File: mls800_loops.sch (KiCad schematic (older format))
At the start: 52 parts, among them J10 JACK_2P_STACK, J11 JACK_2P_SW, J2 JACK_2P_SW, J3 JACK_2P_STACK, J4 JACK_2P_STACK, J5 JACK_2P_STACK, J6 JACK_2P_STACK, J7 JACK_2P_STACK, J8 JACK_2P_STACK, J9 JACK_2P_STACK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

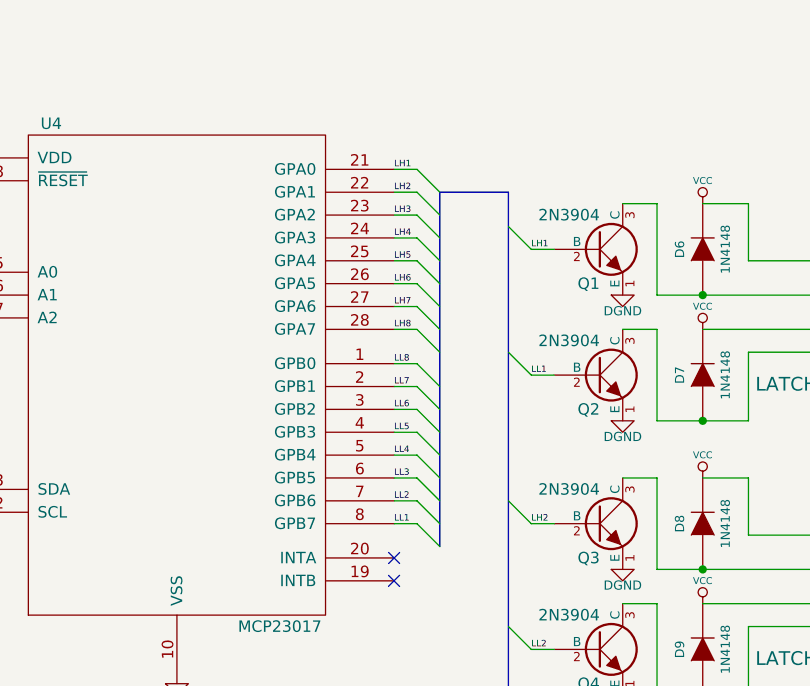
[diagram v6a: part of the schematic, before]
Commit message: MLS800
* routing : core pcb & components
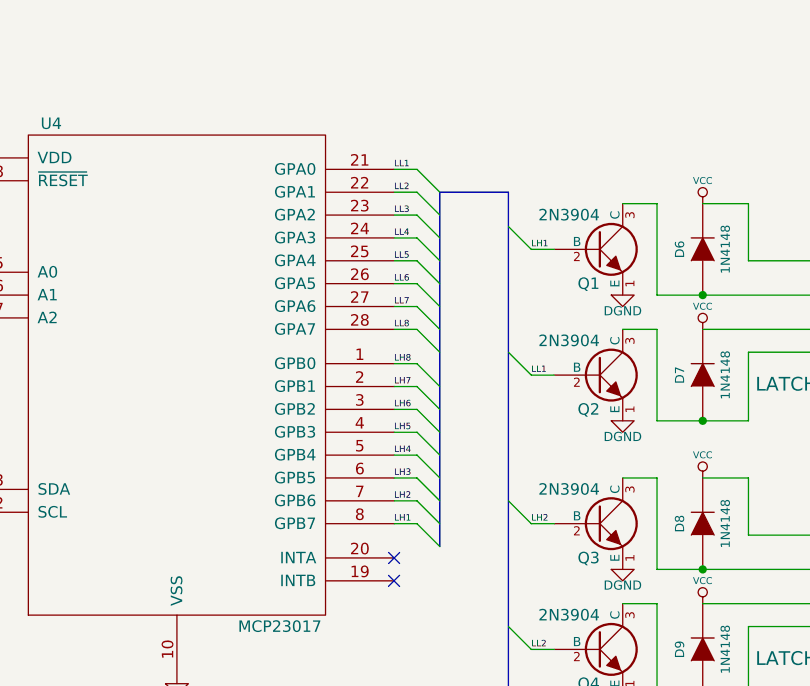
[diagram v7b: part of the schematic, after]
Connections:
- net LH1: now also U4.8 (GPB7); no longer U4.21 (GPA0)
- net LH2: now also U4.7 (GPB6); no longer U4.22 (GPA1)
- net LH3: now also U4.6 (GPB5); no longer U4.23 (GPA2)
- net LH4: now also U4.5 (GPB4); no longer U4.24 (GPA3)
- net LH5: now also U4.4 (GPB3); no longer U4.25 (GPA4)
- net LH6: now also U4.3 (GPB2); no longer U4.26 (GPA5)
- net LH7: now also U4.2 (GPB1); no longer U4.27 (GPA6)
- net LH8: now also U4.1 (GPB0); no longer U4.28 (GPA7)
- net LL1: now also U4.21 (GPA0); no longer U4.8 (GPB7)
- net LL2: now also U4.22 (GPA1); no longer U4.7 (GPB6)
- net LL3: now also U4.23 (GPA2); no longer U4.6 (GPB5)
- net LL4: now also U4.24 (GPA3); no longer U4.5 (GPB4)
- net LL5: now also U4.25 (GPA4); no longer U4.4 (GPB3)
- net LL6: now also U4.26 (GPA5); no longer U4.3 (GPB2)
- net LL7: now also U4.27 (GPA6); no longer U4.2 (GPB1)
- net LL8: now also U4.28 (GPA7); no longer U4.1 (GPB0)
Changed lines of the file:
@@
 	3100 1100 3200 1200
 Text Label 3000 1100 0    28   ~ 0
+LL1
+Text Label 3000 1200 0    28   ~ 0
+LL2
+Text Label 3000 1300 0    28   ~ 0
+LL3
+Text Label 3000 1400 0    28   ~ 0
+LL4
+Text Label 3000 1500 0    28   ~ 0
+LL5
+Text Label 3000 1600 0    28   ~ 0
+LL6
+Text Label 3000 1700 0    28   ~ 0
+LL7
+Text Label 3000 1800 0    28   ~ 0
+LL8
+Text Label 3000 1950 0    28   ~ 0
+LH8
+Text Label 3000 2050 0    28   ~ 0
+LH7
+Text Label 3000 2150 0    28   ~ 0
+LH6
+Text Label 3000 2250 0    28   ~ 0
+LH5
+Text Label 3000 2350 0    28   ~ 0
+LH4
+Text Label 3000 2450 0    28   ~ 0
+LH3
+Text Label 3000 2550 0    28   ~ 0
+LH2
+Text Label 3000 2650 0    28   ~ 0
 LH1
-Text Label 3000 1200 0    28   ~ 0
-LH2
-Text Label 3000 1300 0    28   ~ 0
-LH3
-Text Label 3000 1400 0    28   ~ 0
-LH4
-Text Label 3000 1500 0    28   ~ 0
-LH5
-Text Label 3000 1600 0    28   ~ 0
-LH6
-Text Label 3000 1700 0    28   ~ 0
-LH7
-Text Label 3000 1800 0    28   ~ 0
-LH8
-Text Label 3000 1950 0    28   ~ 0
-LL8
-Text Label 3000 2050 0    28   ~ 0
-LL7
-Text Label 3000 2150 0    28   ~ 0
-LL6
-Text Label 3000 2250 0    28   ~ 0
-LL5
-Text Label 3000 2350 0    28   ~ 0
-LL4
-Text Label 3000 2450 0    28   ~ 0
-LL3
-Text Label 3000 2550 0    28   ~ 0
-LL2
-Text Label 3000 2650 0    28   ~ 0
-LL1
 Text Notes 850  5850 0    197  ~ 39
 LOOPS

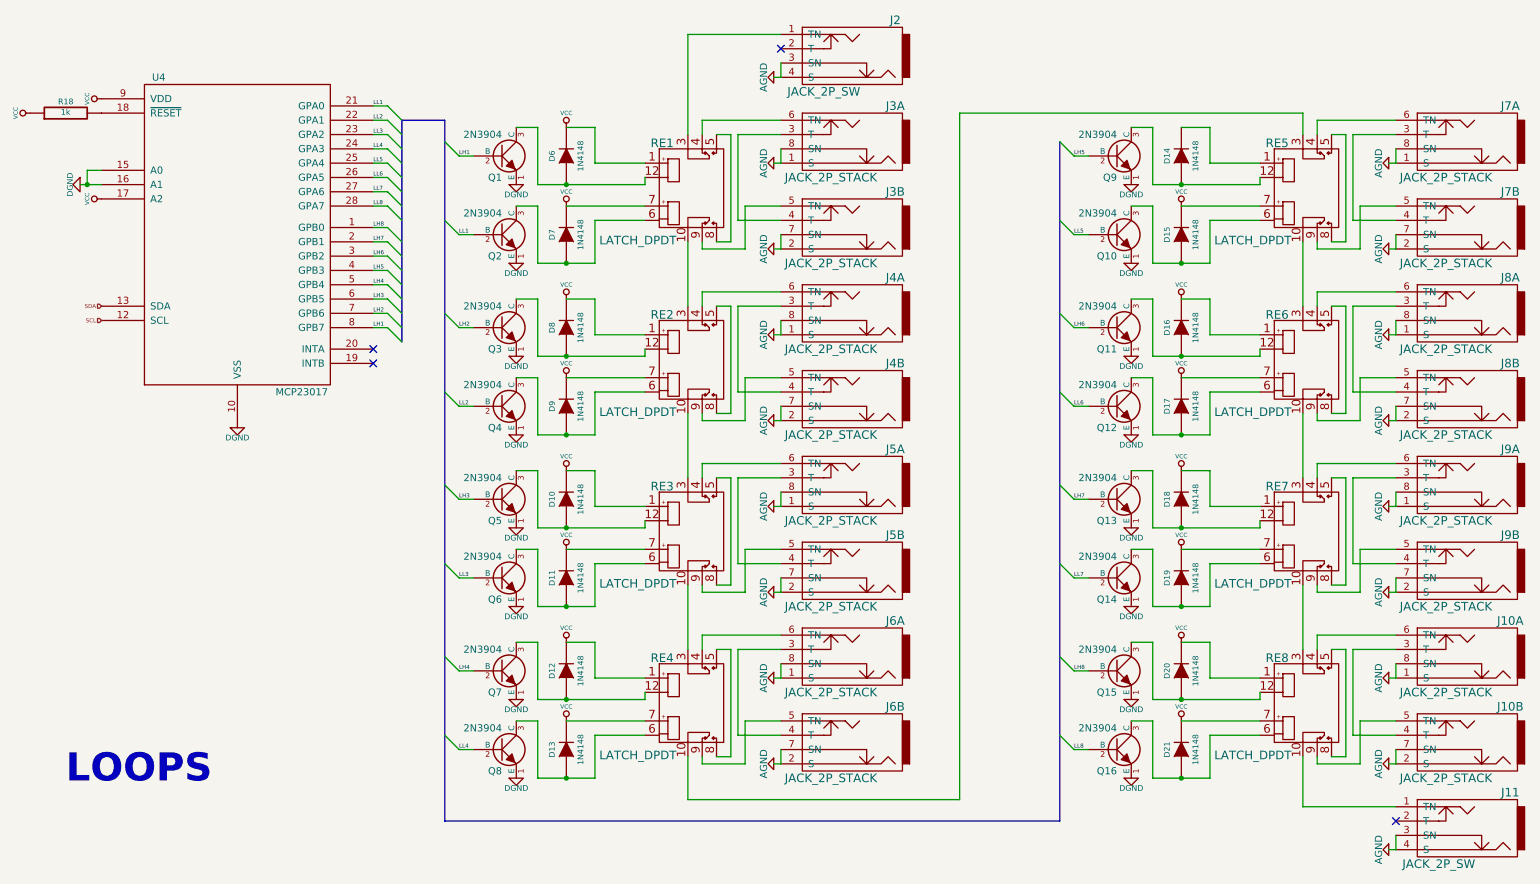
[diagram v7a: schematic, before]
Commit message: MLS800
* schematic : changed all 1n4148 to bournes references
 * changed footprints to match bournes ones
 * re routed all the loops part of the pcb
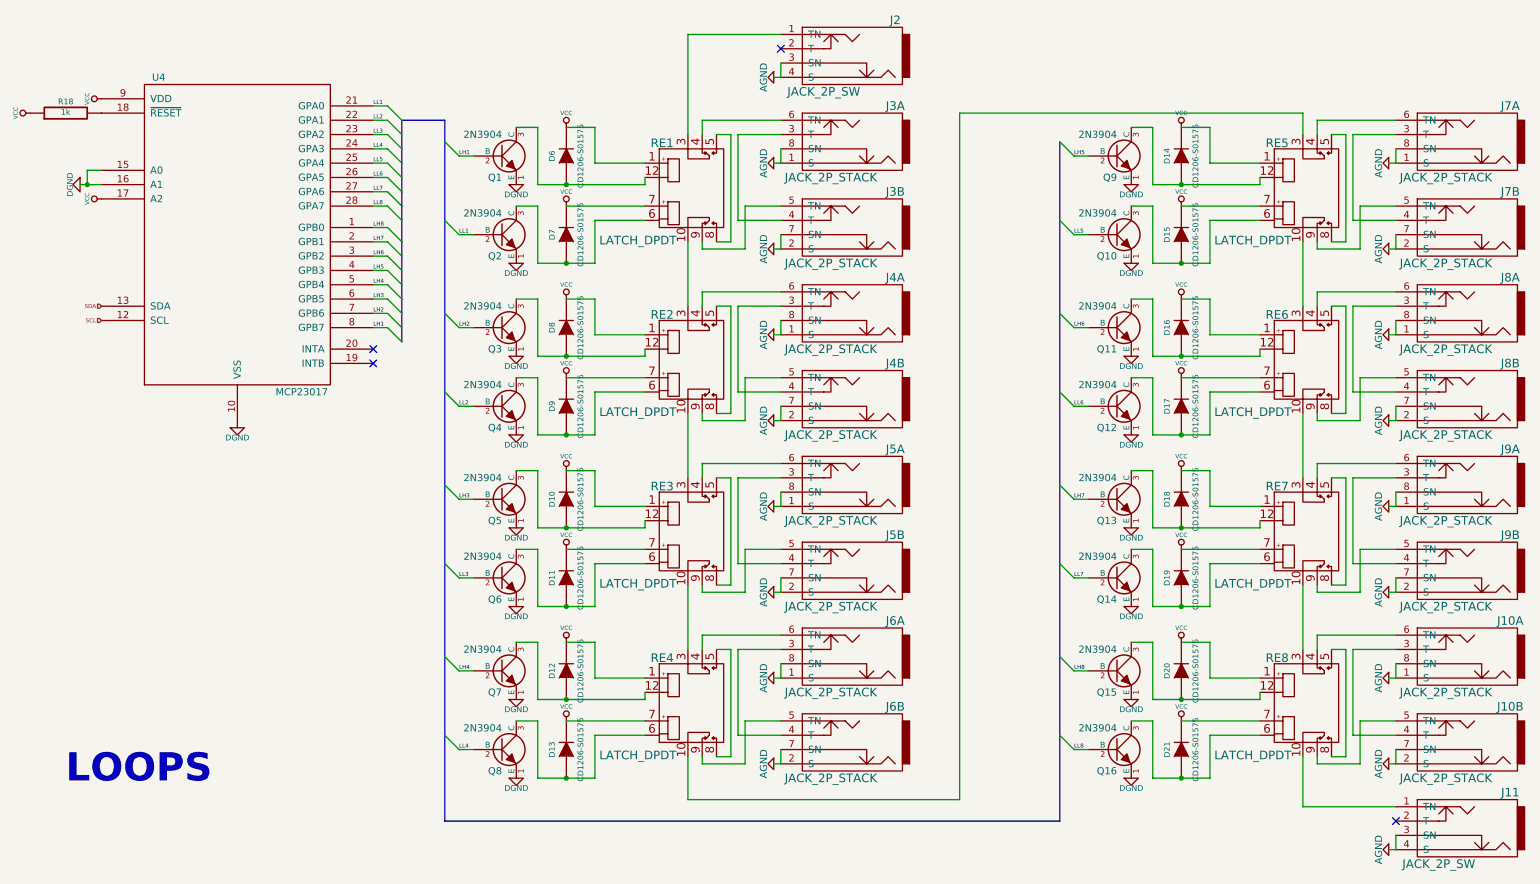
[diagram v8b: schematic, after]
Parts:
- D10, D11, D12, D13, D14, D15, D16, D17, D18, D19, D20, D21, D6, D7, D8, D9: value 1N4148 -> CD1206-S01575; footprint Imported:SOD-123 -> SMD_Packages:SMD-1206_Pol
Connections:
- net VCC: now also D14.2 (K), RE5.1
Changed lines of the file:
@@
 P 4350 1450
 F 0 "D6" H 4350 1550 40  0000 C CNN
-F 1 "1N4148" H 4350 1350 40  0000 C CNN
-F 2 "Imported:SOD-123" H 4350 1450 60  0001 C CNN
+F 1 "CD1206-S01575" H 4350 1350 40  0000 C CNN
+F 2 "SMD_Packages:SMD-1206_Pol" H 4350 1450 60  0001 C CNN
 F 3 "~" H 4350 1450 60  0000 C CNN
 	1    4350 1450
@@
 P 4350 2000
 F 0 "D7" H 4350 2100 40  0000 C CNN
-F 1 "1N4148" H 4350 1900 40  0000 C CNN
-F 2 "Imported:SOD-123" H 4350 2000 60  0001 C CNN
+F 1 "CD1206-S01575" H 4350 1900 40  0000 C CNN
+F 2 "SMD_Packages:SMD-1206_Pol" H 4350 2000 60  0001 C CNN
 F 3 "~" H 4350 2000 60  0000 C CNN
 	1    4350 2000
@@
 P 4350 2650
 F 0 "D8" H 4350 2750 40  0000 C CNN
-F 1 "1N4148" H 4350 2550 40  0000 C CNN
-F 2 "Imported:SOD-123" H 4350 2650 60  0001 C CNN
+F 1 "CD1206-S01575" H 4350 2550 40  0000 C CNN
+F 2 "SMD_Packages:SMD-1206_Pol" H 4350 2650 60  0001 C CNN
 F 3 "~" H 4350 2650 60  0000 C CNN
 	1    4350 2650
@@
 P 4350 3200
 F 0 "D9" H 4350 3300 40  0000 C CNN
-F 1 "1N4148" H 4350 3100 40  0000 C CNN
-F 2 "Imported:SOD-123" H 4350 3200 60  0001 C CNN
+F 1 "CD1206-S01575" H 4350 3100 40  0000 C CNN
+F 2 "SMD_Packages:SMD-1206_Pol" H 4350 3200 60  0001 C CNN
 F 3 "~" H 4350 3200 60  0000 C CNN
 	1    4350 3200
@@
 P 4350 3850
 F 0 "D10" H 4350 3950 40  0000 C CNN
-F 1 "1N4148" H 4350 3750 40  0000 C CNN
-F 2 "Imported:SOD-123" H 4350 3850 60  0001 C CNN
+F 1 "CD1206-S01575" H 4350 3750 40  0000 C CNN
+F 2 "SMD_Packages:SMD-1206_Pol" H 4350 3850 60  0001 C CNN
 F 3 "~" H 4350 3850 60  0000 C CNN
 	1    4350 3850
@@
 P 4350 4400
 F 0 "D11" H 4350 4500 40  0000 C CNN
-F 1 "1N4148" H 4350 4300 40  0000 C CNN
-F 2 "Imported:SOD-123" H 4350 4400 60  0001 C CNN
+F 1 "CD1206-S01575" H 4350 4300 40  0000 C CNN
+F 2 "SMD_Packages:SMD-1206_Pol" H 4350 4400 60  0001 C CNN
 F 3 "~" H 4350 4400 60  0000 C CNN
 	1    4350 4400
@@
 P 4350 5050
 F 0 "D12" H 4350 5150 40  0000 C CNN
-F 1 "1N4148" H 4350 4950 40  0000 C CNN
-F 2 "Imported:SOD-123" H 4350 5050 60  0001 C CNN
+F 1 "CD1206-S01575" H 4350 4950 40  0000 C CNN
+F 2 "SMD_Packages:SMD-1206_Pol" H 4350 5050 60  0001 C CNN
 F 3 "~" H 4350 5050 60  0000 C CNN
 	1    4350 5050
@@
 P 4350 5600
 F 0 "D13" H 4350 5700 40  0000 C CNN
-F 1 "1N4148" H 4350 5500 40  0000 C CNN
-F 2 "Imported:SOD-123" H 4350 5600 60  0001 C CNN
+F 1 "CD1206-S01575" H 4350 5500 40  0000 C CNN
+F 2 "SMD_Packages:SMD-1206_Pol" H 4350 5600 60  0001 C CNN
 F 3 "~" H 4350 5600 60  0000 C CNN
 	1    4350 5600
@@
 P 8650 1450
 F 0 "D14" H 8650 1550 40  0000 C CNN
-F 1 "1N4148" H 8650 1350 40  0000 C CNN
-F 2 "Imported:SOD-123" H 8650 1450 60  0001 C CNN
+F 1 "CD1206-S01575" H 8650 1350 40  0000 C CNN
+F 2 "SMD_Packages:SMD-1206_Pol" H 8650 1450 60  0001 C CNN
 F 3 "~" H 8650 1450 60  0000 C CNN
 	1    8650 1450
@@
 P 8650 2000
 F 0 "D15" H 8650 2100 40  0000 C CNN
-F 1 "1N4148" H 8650 1900 40  0000 C CNN
-F 2 "Imported:SOD-123" H 8650 2000 60  0001 C CNN
+F 1 "CD1206-S01575" H 8650 1900 40  0000 C CNN
+F 2 "SMD_Packages:SMD-1206_Pol" H 8650 2000 60  0001 C CNN
 F 3 "~" H 8650 2000 60  0000 C CNN
 	1    8650 2000
@@
 P 8650 2650
 F 0 "D16" H 8650 2750 40  0000 C CNN
-F 1 "1N4148" H 8650 2550 40  0000 C CNN
-F 2 "Imported:SOD-123" H 8650 2650 60  0001 C CNN
+F 1 "CD1206-S01575" H 8650 2550 40  0000 C CNN
+F 2 "SMD_Packages:SMD-1206_Pol" H 8650 2650 60  0001 C CNN
 F 3 "~" H 8650 2650 60  0000 C CNN
 	1    8650 2650
@@
 P 8650 3200
 F 0 "D17" H 8650 3300 40  0000 C CNN
-F 1 "1N4148" H 8650 3100 40  0000 C CNN
-F 2 "Imported:SOD-123" H 8650 3200 60  0001 C CNN
+F 1 "CD1206-S01575" H 8650 3100 40  0000 C CNN
+F 2 "SMD_Packages:SMD-1206_Pol" H 8650 3200 60  0001 C CNN
 F 3 "~" H 8650 3200 60  0000 C CNN
 	1    8650 3200
@@
 P 8650 3850
 F 0 "D18" H 8650 3950 40  0000 C CNN
-F 1 "1N4148" H 8650 3750 40  0000 C CNN
-F 2 "Imported:SOD-123" H 8650 3850 60  0001 C CNN
+F 1 "CD1206-S01575" H 8650 3750 40  0000 C CNN
+F 2 "SMD_Packages:SMD-1206_Pol" H 8650 3850 60  0001 C CNN
 F 3 "~" H 8650 3850 60  0000 C CNN
 	1    8650 3850
@@
 P 8650 4400
 F 0 "D19" H 8650 4500 40  0000 C CNN
-F 1 "1N4148" H 8650 4300 40  0000 C CNN
-F 2 "Imported:SOD-123" H 8650 4400 60  0001 C CNN
+F 1 "CD1206-S01575" H 8650 4300 40  0000 C CNN
+F 2 "SMD_Packages:SMD-1206_Pol" H 8650 4400 60  0001 C CNN
 F 3 "~" H 8650 4400 60  0000 C CNN
 	1    8650 4400
@@
 P 8650 5050
 F 0 "D20" H 8650 5150 40  0000 C CNN
-F 1 "1N4148" H 8650 4950 40  0000 C CNN
-F 2 "Imported:SOD-123" H 8650 5050 60  0001 C CNN
+F 1 "CD1206-S01575" H 8650 4950 40  0000 C CNN
+F 2 "SMD_Packages:SMD-1206_Pol" H 8650 5050 60  0001 C CNN
 F 3 "~" H 8650 5050 60  0000 C CNN
 	1    8650 5050
@@
 P 8650 5600
 F 0 "D21" H 8650 5700 40  0000 C CNN
-F 1 "1N4148" H 8650 5500 40  0000 C CNN
-F 2 "Imported:SOD-123" H 8650 5600 60  0001 C CNN
+F 1 "CD1206-S01575" H 8650 5500 40  0000 C CNN
+F 2 "SMD_Packages:SMD-1206_Pol" H 8650 5600 60  0001 C CNN
 F 3 "~" H 8650 5600 60  0000 C CNN
 	1    8650 5600
@@
 	0    -1   -1   0
 $EndComp
+$Comp
+L VCC #PWR?
+U 1 1 54AB5125
+P 8650 1250
+F 0 "#PWR?" H 8650 1350 30  0001 C CNN
+F 1 "VCC" H 8650 1350 30  0000 C CNN
+F 2 "" H 8650 1250 60  0000 C CNN
+F 3 "" H 8650 1250 60  0000 C CNN
+	1    8650 1250
+	1    0    0    -1
+$EndComp
 $EndSCHEMATC
